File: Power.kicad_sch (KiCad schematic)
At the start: 23 parts, among them J10 Servo PW 7, J11 Servo PW 8, J3 1986660-2, J4 Servo PW 1, J5 Servo PW 2, J6 Servo PW 3, J7 Servo PW 4, J8 Servo PW 5, J9 Servo PW 6, U4 AP62301WU

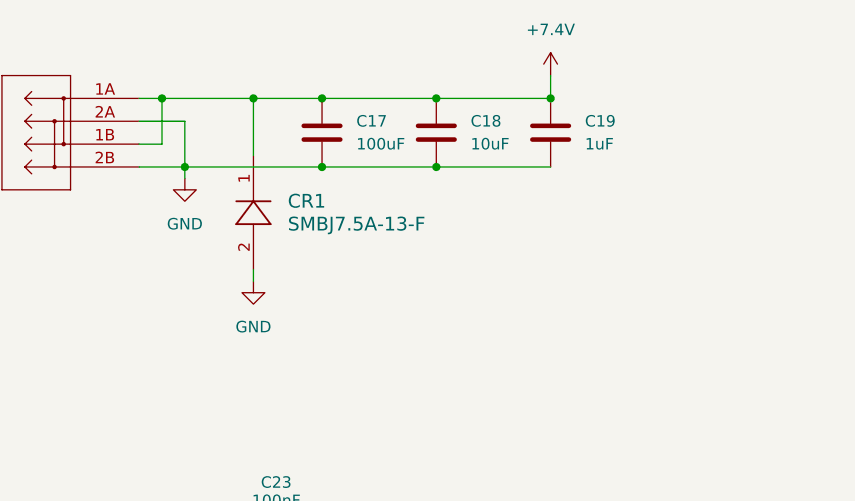
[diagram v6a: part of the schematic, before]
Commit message: Add Schottky diode
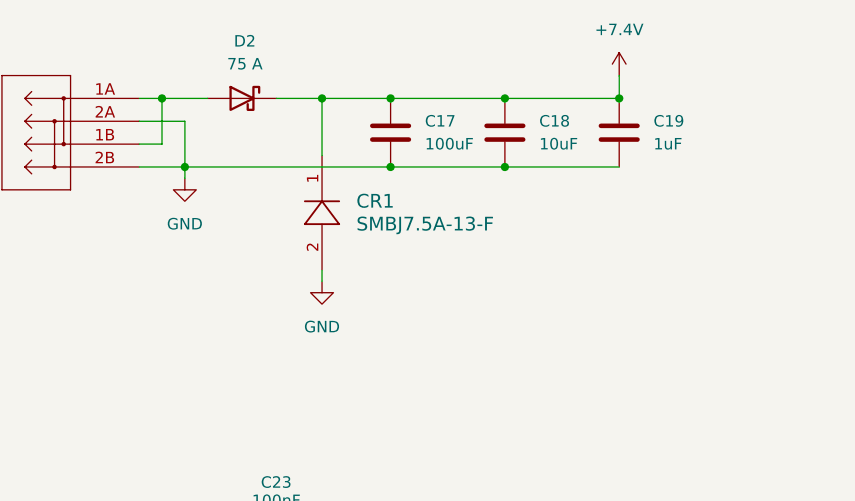
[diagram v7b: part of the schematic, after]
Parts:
- added D2: 75 A, Package_TO_SOT_THT:TO-247-2_Vertical, symbol Device:D_Schottky
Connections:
- net +7.4V: now also D2.1 (K); no longer J3.1A, J3.1B
- new net: D2.2 (A), J3.1A, J3.1B
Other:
- moved on the sheet: C17, C18, C19, CR1
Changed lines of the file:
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@@
 	)
 	(junction
-		(at 88.9 48.26)
+		(at 96.52 48.26)
 		(diameter 0)
 		(color 0 0 0 0)
@@
 	)
 	(junction
-		(at 88.9 40.64)
+		(at 96.52 40.64)
 		(diameter 0)
 		(color 0 0 0 0)
 	)
 	(junction
-		(at 76.2 48.26)
+		(at 83.82 48.26)
 		(diameter 0)
 		(color 0 0 0 0)
 	)
 	(junction
-		(at 76.2 40.64)
+		(at 83.82 40.64)
 		(diameter 0)
 		(color 0 0 0 0)
@@
 	)
 	(junction
-		(at 68.58 40.64)
+		(at 76.2 40.64)
 		(diameter 0)
 		(color 0 0 0 0)
@@
 	)
 	(junction
-		(at 101.6 40.64)
+		(at 109.22 40.64)
 		(diameter 0)
 		(color 0 0 0 0)
@@
 	(wire
 		(pts
-			(xy 58.42 40.64) (xy 68.58 40.64)
+			(xy 58.42 40.64) (xy 63.5 40.64)
 		)
 		(stroke
@@
 	(wire
 		(pts
+			(xy 71.12 40.64) (xy 76.2 40.64)
+		)
+		(stroke
+			(width 0)
+			(type default)
+		)
+	)
+	(wire
+		(pts
 			(xy 143.51 114.3) (xy 127 114.3)
 		)
@@
 	(wire
 		(pts
-			(xy 68.58 40.64) (xy 68.58 46.99)
+			(xy 76.2 40.64) (xy 76.2 46.99)
 		)
 		(stroke
@@
 	(wire
 		(pts
-			(xy 68.58 59.69) (xy 68.58 60.96)
+			(xy 76.2 59.69) (xy 76.2 60.96)
 		)
 		(stroke
@@
 	(wire
 		(pts
-			(xy 88.9 40.64) (xy 101.6 40.64)
+			(xy 96.52 40.64) (xy 109.22 40.64)
 		)
 		(stroke
@@
 	(wire
 		(pts
-			(xy 76.2 48.26) (xy 88.9 48.26)
+			(xy 83.82 48.26) (xy 96.52 48.26)
 		)
 		(stroke
@@
 	(wire
 		(pts
-			(xy 88.9 48.26) (xy 101.6 48.26)
+			(xy 96.52 48.26) (xy 109.22 48.26)
 		)
 		(stroke
@@
 	(wire
 		(pts
-			(xy 101.6 38.1) (xy 101.6 40.64)
+			(xy 109.22 38.1) (xy 109.22 40.64)
 		)
 		(stroke
@@
 	(wire
 		(pts
-			(xy 76.2 40.64) (xy 88.9 40.64)
+			(xy 83.82 40.64) (xy 96.52 40.64)
 		)
 		(stroke
@@
 	(wire
 		(pts
-			(xy 60.96 48.26) (xy 76.2 48.26)
+			(xy 60.96 48.26) (xy 83.82 48.26)
 		)
 		(stroke
@@
 	(wire
 		(pts
-			(xy 68.58 40.64) (xy 76.2 40.64)
+			(xy 76.2 40.64) (xy 83.82 40.64)
 		)
 		(stroke
@@
 	(symbol
 		(lib_id "Device:C")
-		(at 101.6 44.45 0)
+		(at 109.22 44.45 0)
 		(unit 1)
 		(exclude_from_sim no)
@@
 		(fields_autoplaced yes)
 		(property "Reference" "C19"
-			(at 105.41 43.1799 0)
+			(at 113.03 43.1799 0)
 			(effects
 				(font
@@
 		)
 		(property "Value" "1uF"
-			(at 105.41 45.7199 0)
+			(at 113.03 45.7199 0)
 			(effects
 				(font
@@
 		)
 		(property "Footprint" ""
-			(at 102.5652 48.26 0)
+			(at 110.1852 48.26 0)
 			(effects
 				(font
@@
 		)
 		(property "Datasheet" "~"
-			(at 101.6 44.45 0)
+			(at 109.22 44.45 0)
 			(effects
 				(font
@@
 		)
 		(property "Description" "Unpolarized capacitor"
-			(at 101.6 44.45 0)
+			(at 109.22 44.45 0)
 			(effects
 				(font
@@
 	(symbol
 		(lib_id "power:GND")
-		(at 68.58 60.96 0)
+		(at 76.2 60.96 0)
 		(unit 1)
 		(exclude_from_sim no)
@@
 		(fields_autoplaced yes)
 		(property "Reference" "#PWR045"
-			(at 68.58 67.31 0)
+			(at 76.2 67.31 0)
 			(effects
 				(font
@@
 		)
 		(property "Value" "GND"
-			(at 68.58 66.04 0)
+			(at 76.2 66.04 0)
 			(effects
 				(font
@@
 		)
 		(property "Footprint" ""
-			(at 68.58 60.96 0)
+			(at 76.2 60.96 0)
 			(effects
 				(font
@@
 		)
 		(property "Datasheet" ""
-			(at 68.58 60.96 0)
+			(at 76.2 60.96 0)
 			(effects
 				(font
@@
 		)
 		(property "Description" "Power symbol creates a global label with name \"GND\" , ground"
-			(at 68.58 60.96 0)
+			(at 76.2 60.96 0)
 			(effects
 				(font
@@
 	)
 	(symbol
+		(lib_id "Device:D_Schottky")
+		(at 67.31 40.64 0)
+		(mirror y)
+		(unit 1)
+		(exclude_from_sim no)
+		(in_bom yes)
+		(on_board yes)
+		(dnp no)
+		(property "Reference" "D2"
+			(at 67.6275 34.29 0)
+			(effects
+				(font
+					(size 1.27 1.27)
+				)
+			)
+		)
+		(property "Value" "75 A"
+			(at 67.6275 36.83 0)
+			(effects
+				(font
+					(size 1.27 1.27)
+				)
+			)
+		)
+		(property "Footprint" "Package_TO_SOT_THT:TO-247-2_Vertical"
+			(at 67.31 40.64 0)
+			(effects
+				(font
+					(size 1.27 1.27)
+				)
+				(hide yes)
+			)
+		)
+		(property "Datasheet" "https://ww1.microchip.com/downloads/en/DeviceDoc/APT60S20B_S(G)_E.PDF"
+			(at 67.31 40.64 0)
+			(effects
+				(font
+					(size 1.27 1.27)
+				)
+				(hide yes)
+			)
+		)
+		(property "Description" "Schottky diode - APT60S20BG"
+			(at 67.31 40.64 0)
+			(effects
+				(font
+					(size 1.27 1.27)
+				)
+				(hide yes)
+			)
+		)
+		(pin "1"
+		)
+		(pin "2"
+		)
+		(instances
+			(project ""
+				(path "/71bb14ae-b730-4d22-a41d-cf68989dae2d/16595639-dffe-4aa9-8e36-79b79804718e"
+					(reference "D2")
+					(unit 1)
+				)
+			)
+		)
+	)
+	(symbol
 		(lib_id "power:+7.5V")
-		(at 101.6 38.1 0)
+		(at 109.22 38.1 0)
 		(unit 1)
 		(exclude_from_sim no)
@@
 		(fields_autoplaced yes)
 		(property "Reference" "#PWR039"
-			(at 101.6 41.91 0)
+			(at 109.22 41.91 0)
 			(effects
 				(font
@@
 		)
 		(property "Value" "+7.4V"
-			(at 101.6 33.02 0)
+			(at 109.22 33.02 0)
 			(effects
 				(font
@@
 		)
 		(property "Footprint" ""
-			(at 101.6 38.1 0)
+			(at 109.22 38.1 0)
 			(effects
 				(font
@@
 		)
 		(property "Datasheet" ""
-			(at 101.6 38.1 0)
+			(at 109.22 38.1 0)
 			(effects
 				(font
@@
 		)
 		(property "Description" "Power symbol creates a global label with name \"+7.5V\""
-			(at 101.6 38.1 0)
+			(at 109.22 38.1 0)
 			(effects
 				(font
@@
 	(symbol
 		(lib_id "Device:C")
-		(at 76.2 44.45 0)
+		(at 83.82 44.45 0)
 		(unit 1)
 		(exclude_from_sim no)
@@
 		(fields_autoplaced yes)
 		(property "Reference" "C17"
-			(at 80.01 43.1799 0)
+			(at 87.63 43.1799 0)
 			(effects
 				(font
@@
 		)
 		(property "Value" "100uF"
-			(at 80.01 45.7199 0)
+			(at 87.63 45.7199 0)
 			(effects
 				(font
@@
 		)
 		(property "Footprint" ""
-			(at 77.1652 48.26 0)
+			(at 84.7852 48.26 0)
 			(effects
 				(font
@@
 		)
 		(property "Datasheet" "~"
-			(at 76.2 44.45 0)
+			(at 83.82 44.45 0)
 			(effects
 				(font
@@
 		)
 		(property "Description" "Unpolarized capacitor"
-			(at 76.2 44.45 0)
+			(at 83.82 44.45 0)
 			(effects
 				(font
@@
 	(symbol
 		(lib_id "Device:C")
-		(at 88.9 44.45 0)
+		(at 96.52 44.45 0)
 		(unit 1)
 		(exclude_from_sim no)
@@
 		(fields_autoplaced yes)
 		(property "Reference" "C18"
-			(at 92.71 43.1799 0)
+			(at 100.33 43.1799 0)
 			(effects
 				(font
@@
 		)
 		(property "Value" "10uF"
-			(at 92.71 45.7199 0)
+			(at 100.33 45.7199 0)
 			(effects
 				(font
@@
 		)
 		(property "Footprint" ""
-			(at 89.8652 48.26 0)
+			(at 97.4852 48.26 0)
 			(effects
 				(font
@@
 		)
 		(property "Datasheet" "~"
-			(at 88.9 44.45 0)
+			(at 96.52 44.45 0)
 			(effects
 				(font
@@
 		)
 		(property "Description" "Unpolarized capacitor"
-			(at 88.9 44.45 0)
+			(at 96.52 44.45 0)
 			(effects
 				(font
@@
 	(symbol
 		(lib_id "XuLab:SMBJ7.5A-13-F")
-		(at 68.58 53.34 90)
+		(at 76.2 53.34 90)
 		(unit 1)
 		(exclude_from_sim no)
@@
 		(fields_autoplaced yes)
 		(property "Reference" "CR1"
-			(at 72.39 52.0699 90)
+			(at 80.01 52.0699 90)
 			(effects
 				(font
@@
 		)
 		(property "Value" "SMBJ7.5A-13-F"
-			(at 72.39 54.6099 90)
+			(at 80.01 54.6099 90)
 			(effects
 				(font
@@
 		)
 		(property "Footprint" "XuLab:SMB_DIO"
-			(at 77.216 53.594 0)
+			(at 84.836 53.594 0)
 			(effects
 				(font
@@
 		)
 		(property "Datasheet" "https://www.diodes.com/assets/Datasheets/ds19002.pdf"
-			(at 74.93 53.594 0)
+			(at 82.55 53.594 0)
 			(effects
 				(font
@@
 		)
 		(property "Description" "7.5 V Reverse Standoff TVS"
-			(at 68.58 53.34 0)
+			(at 76.2 53.34 0)
 			(effects
 				(font

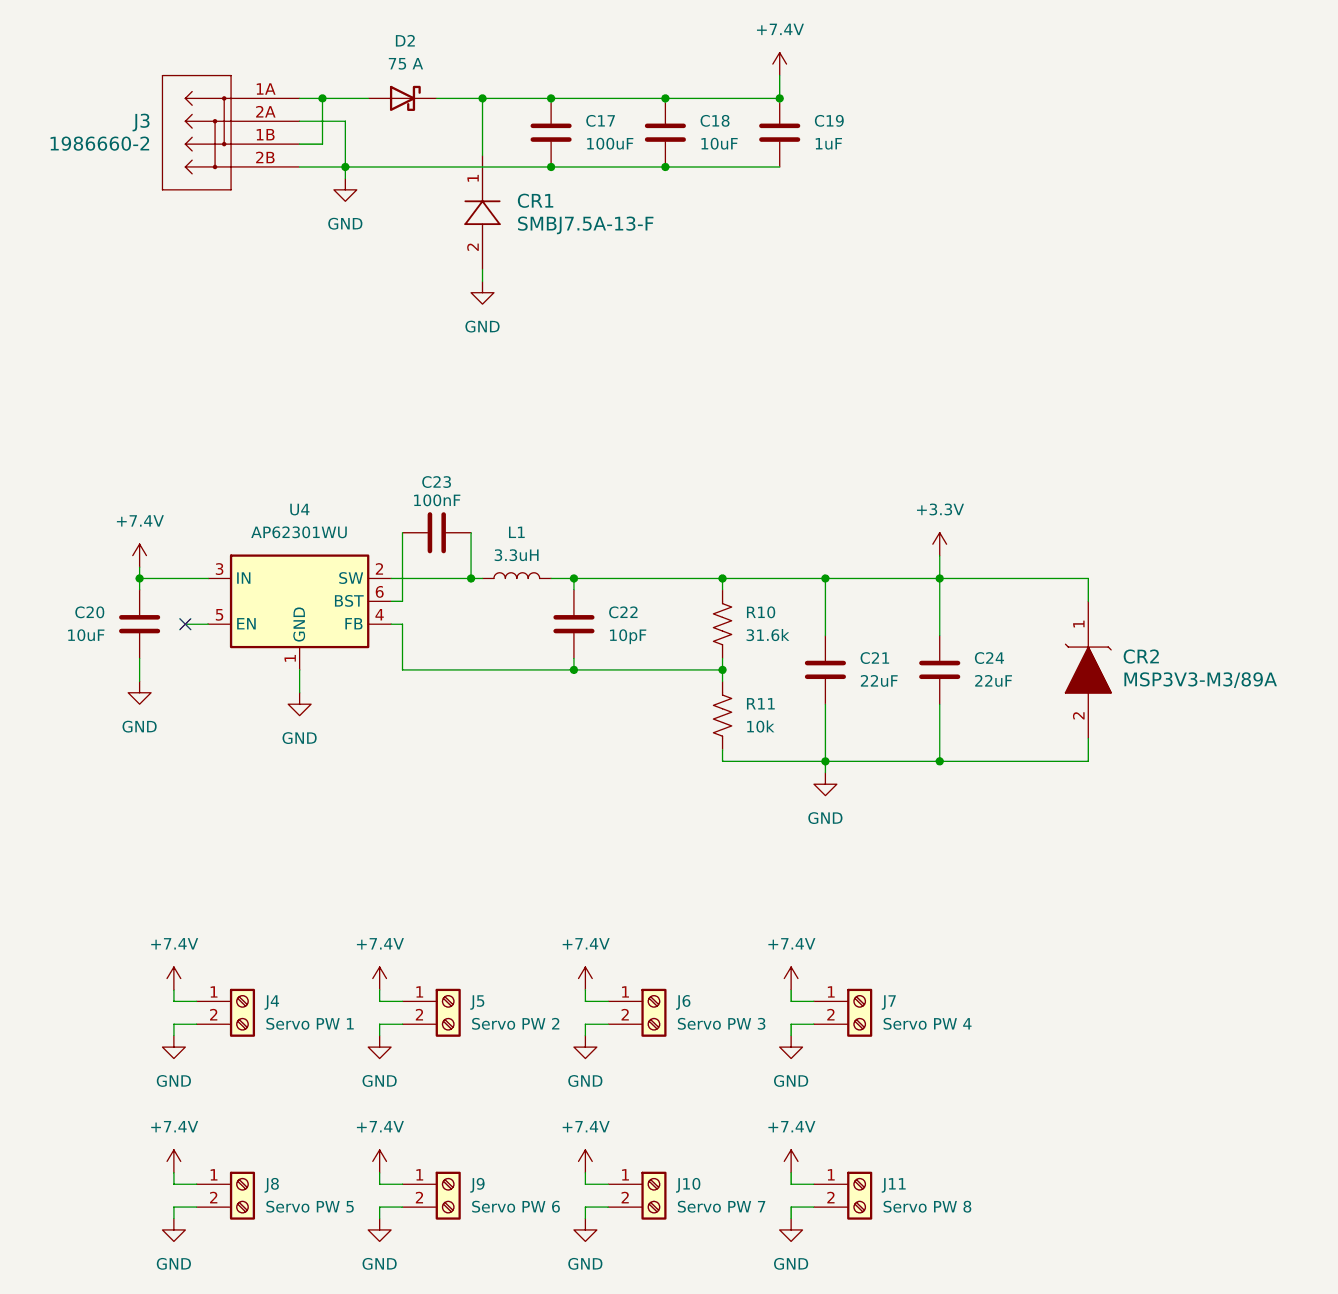
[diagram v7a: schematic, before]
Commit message: Fix duplicate capacitor labels
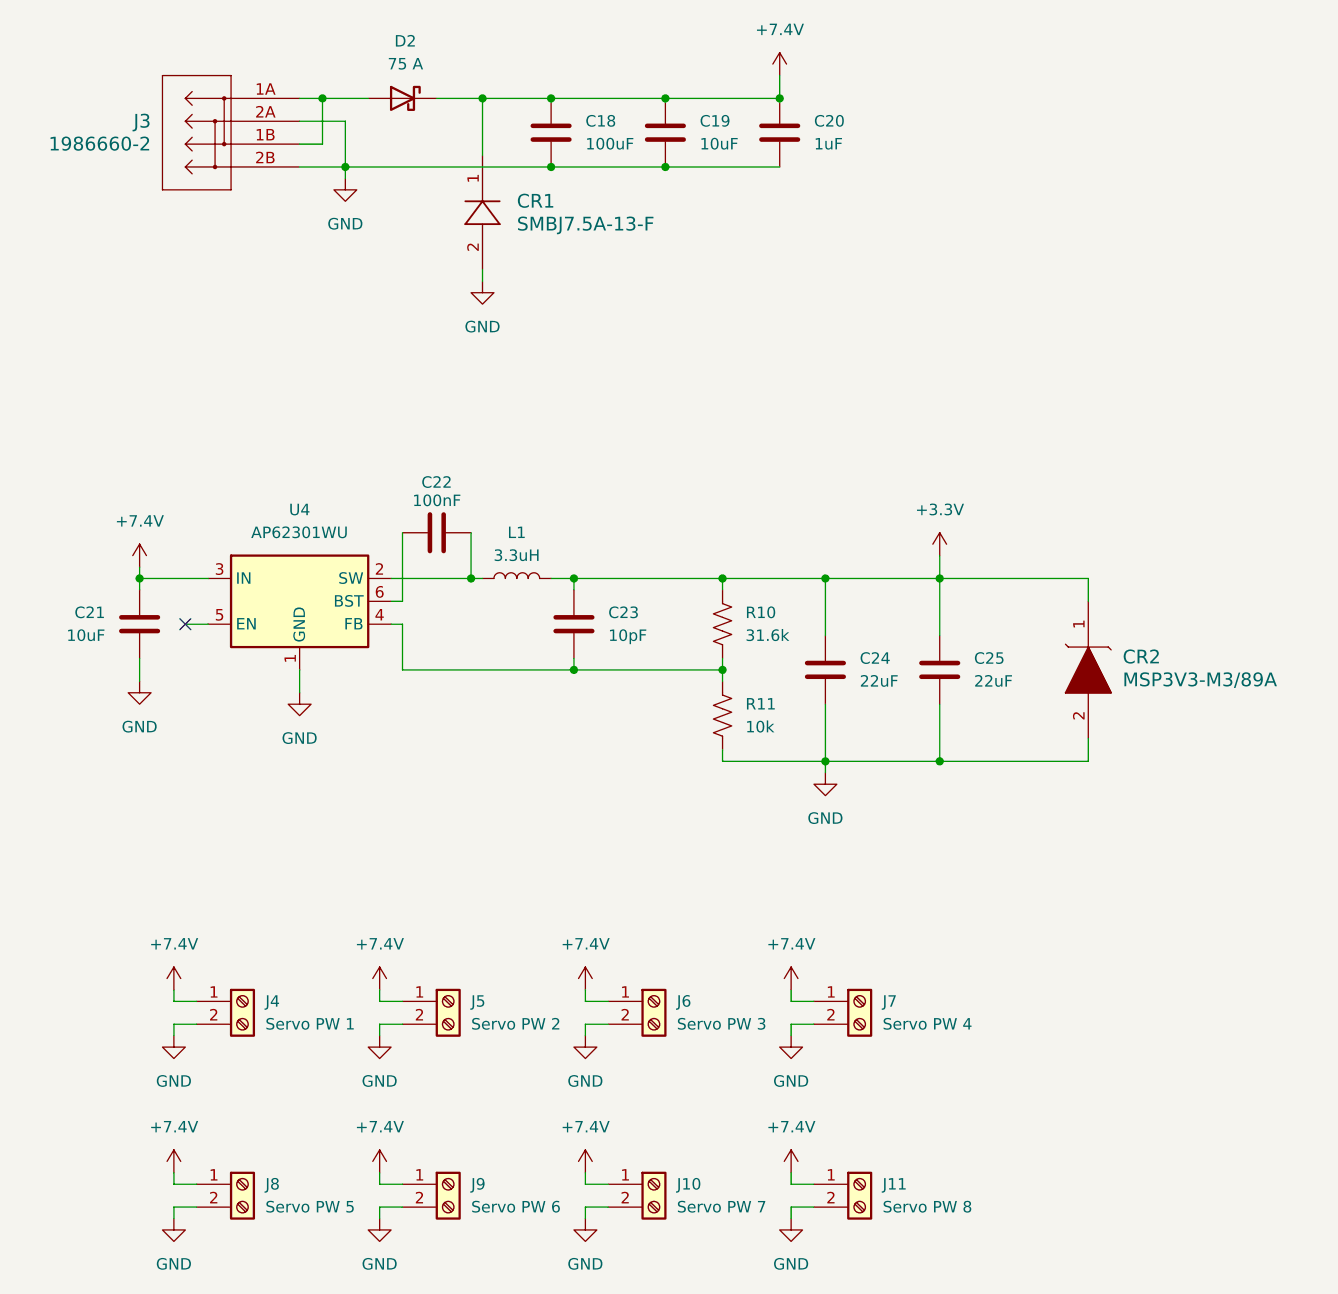
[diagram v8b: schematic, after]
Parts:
- renumbered C17 to C18, C18 to C19, C19 to C20, C20 to C21, C23 to C22, C22 to C23, C21 to C24, C24 to C25
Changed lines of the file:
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@@
 		(dnp no)
 		(fields_autoplaced yes)
-		(property "Reference" "C19"
+		(property "Reference" "C20"
 			(at 113.03 43.1799 0)
 			(effects
@@
 			(project "XuLabPlatform"
 				(path "/71bb14ae-b730-4d22-a41d-cf68989dae2d/16595639-dffe-4aa9-8e36-79b79804718e"
-					(reference "C19")
+					(reference "C20")
 					(unit 1)
 				)
@@
 		(on_board yes)
 		(dnp no)
-		(property "Reference" "C22"
+		(property "Reference" "C23"
 			(at 90.17 97.7899 0)
 			(effects
@@
 			(project "XuLabPlatform"
 				(path "/71bb14ae-b730-4d22-a41d-cf68989dae2d/16595639-dffe-4aa9-8e36-79b79804718e"
-					(reference "C22")
+					(reference "C23")
 					(unit 1)
 				)
@@
 		(on_board yes)
 		(dnp no)
-		(property "Reference" "C21"
+		(property "Reference" "C24"
 			(at 118.11 102.8699 0)
 			(effects
@@
 			(project "XuLabPlatform"
 				(path "/71bb14ae-b730-4d22-a41d-cf68989dae2d/16595639-dffe-4aa9-8e36-79b79804718e"
-					(reference "C21")
+					(reference "C24")
 					(unit 1)
 				)
@@
 		(dnp no)
 		(fields_autoplaced yes)
-		(property "Reference" "C17"
+		(property "Reference" "C18"
 			(at 87.63 43.1799 0)
 			(effects
@@
 			(project ""
 				(path "/71bb14ae-b730-4d22-a41d-cf68989dae2d/16595639-dffe-4aa9-8e36-79b79804718e"
-					(reference "C17")
+					(reference "C18")
 					(unit 1)
 				)
@@
 		(on_board yes)
 		(dnp no)
-		(property "Reference" "C20"
+		(property "Reference" "C21"
 			(at 34.29 97.7899 0)
 			(effects
@@
 			(project "XuLabPlatform"
 				(path "/71bb14ae-b730-4d22-a41d-cf68989dae2d/16595639-dffe-4aa9-8e36-79b79804718e"
-					(reference "C20")
+					(reference "C21")
 					(unit 1)
 				)
@@
 		(on_board yes)
 		(dnp no)
-		(property "Reference" "C24"
+		(property "Reference" "C25"
 			(at 130.81 102.8699 0)
 			(effects
@@
 			(project "XuLabPlatform"
 				(path "/71bb14ae-b730-4d22-a41d-cf68989dae2d/16595639-dffe-4aa9-8e36-79b79804718e"
-					(reference "C24")
+					(reference "C25")
 					(unit 1)
 				)
@@
 		(on_board yes)
 		(dnp no)
-		(property "Reference" "C23"
+		(property "Reference" "C22"
 			(at 71.12 83.312 90)
 			(effects
@@
 			(project "XuLabPlatform"
 				(path "/71bb14ae-b730-4d22-a41d-cf68989dae2d/16595639-dffe-4aa9-8e36-79b79804718e"
-					(reference "C23")
+					(reference "C22")
 					(unit 1)
 				)
@@
 		(dnp no)
 		(fields_autoplaced yes)
-		(property "Reference" "C18"
+		(property "Reference" "C19"
 			(at 100.33 43.1799 0)
 			(effects
@@
 			(project "XuLabPlatform"
 				(path "/71bb14ae-b730-4d22-a41d-cf68989dae2d/16595639-dffe-4aa9-8e36-79b79804718e"
-					(reference "C18")
-					(unit 1)
-				)
+					(reference "C19")
+					(unit 1)
+				)
